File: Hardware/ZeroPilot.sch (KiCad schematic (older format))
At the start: 2 parts

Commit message: Reconfiguring pinout round 2
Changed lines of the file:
@@
-$EndSheet
-$Sheet
-S 4700 3100 1750 3100
-U 5918F046
-F0 "Sheet5918F045" 60
-F1 "STM32F7 IO.sch" 60
-F2 "PPM" I R 6450 3400 60
-F3 "OC[1..12]" O R 6450 3300 60
-F4 "TRACED" I R 6450 3700 60
-F5 "SWDIO" B R 6450 3800 60
-F6 "SWCLK" I R 6450 3900 60
-F7 "TDI" I R 6450 4000 60
-F8 "TDO" I R 6450 4100 60
-F9 "TRACECLK" I R 6450 3600 60
-F10 "NRST" I R 6450 4200 60
-F11 "I2C2_SDA" B R 6450 5350 60
-F12 "I2C2_SCL" B R 6450 5450 60
-F13 "SPI5_MISO" B L 4700 5650 60
-F14 "SPI5_MOSI" B L 4700 5750 60
-F15 "SPI5_SCK" B L 4700 5850 60
-F16 "USART2_TX" O L 4700 3400 60
-F17 "USART2_RX" I L 4700 3500 60
-F18 "SPI1_SCK" B L 4700 4800 60
-F19 "SPI1_MISO" B L 4700 4600 60
-F20 "SPI1_MOSI" B L 4700 4700 60
-F21 "I2C4_SCL" B R 6450 5750 60
-F22 "I2C4_SDA" B R 6450 5650 60
-F23 "UART7_TX" O L 4700 4350 60
-F24 "UART7_RX" I L 4700 4450 60
-F25 "SPI4_SCK" B L 4700 5500 60
-F26 "SPI4_MISO" B L 4700 5300 60
-F27 "SPI4_MOSI" B L 4700 5400 60
-F28 "USART1_RX" I L 4700 3250 60
-F29 "USART1_TX" O L 4700 3150 60
-F30 "USART3_TX" O L 4700 3750 60
-F31 "USART3_RX" I L 4700 3850 60
-F32 "USART3_CK" O L 4700 3950 60
-F33 "SPI3_SCK" B L 4700 5150 60
-F34 "SPI3_MISO" B L 4700 4950 60
-F35 "SPI3_MOSI" B L 4700 5050 60
-F36 "UART4_RX" I L 4700 4200 60
-F37 "UART4_TX" O L 4700 4100 60
-F38 "I2C1_SDA" B R 6450 5050 60
-F39 "I2C1_SCL" B R 6450 5150 60
-F40 "VDD" I R 6450 4450 60
-F41 "USART2_CK" I L 4700 3600 60
-F42 "ADC2_IN8" I R 6450 4600 60
-F43 "ADC2_IN9" I R 6450 4700 60
-F44 "ADC3_IN10" I R 6450 4800 60
-F45 "ADC3_IN11" I R 6450 4900 60
-F46 "TIM10_CH1" I R 6450 5950 60
-F47 "TIM11_CH1" I R 6450 6050 60
 $EndSheet
 $Sheet
@@
 F1 "HEADERS.sch" 60
 $EndSheet
+$Sheet
+S 4700 3100 1750 3450
+U 5918F046
+F0 "Sheet5918F045" 60
+F1 "STM32F7 IO.sch" 60
+F2 "PPM" I R 6450 3400 60
+F3 "OC[1..12]" O R 6450 3300 60
+F4 "SWDIO" B R 6450 3800 60
+F5 "SWCLK" I R 6450 3900 60
+F6 "TDI" I R 6450 4000 60
+F7 "TDO" I R 6450 4100 60
+F8 "NRST" I R 6450 4200 60
+F9 "I2C2_SDA" B R 6450 5350 60
+F10 "I2C2_SCL" B R 6450 5450 60
+F11 "I2C4_SCL" B R 6450 5750 60
+F12 "I2C4_SDA" B R 6450 5650 60
+F13 "I2C1_SDA" B R 6450 5050 60
+F14 "I2C1_SCL" B R 6450 5150 60
+F15 "VDD" I R 6450 4450 60
+F16 "ADC2_IN8" I R 6450 4600 60
+F17 "ADC2_IN9" I R 6450 4700 60
+F18 "ADC3_IN10" I R 6450 4800 60
+F19 "ADC3_IN11" I R 6450 4900 60
+F20 "TIM10_CH1" I R 6450 5950 60
+F21 "TIM11_CH1" I R 6450 6050 60
+F22 "SPI5_MISO" B L 4700 6250 60
+F23 "SPI5_MOSI" B L 4700 6350 60
+F24 "SPI5_SCK" B L 4700 6150 60
+F25 "USART2_TX" O L 4700 3150 60
+F26 "USART2_RX" I L 4700 3250 60
+F27 "SPI1_SCK" B L 4700 5150 60
+F28 "SPI1_MISO" B L 4700 5250 60
+F29 "SPI1_MOSI" B L 4700 5350 60
+F30 "UART7_TX" O L 4700 4700 60
+F31 "UART7_RX" I L 4700 4800 60
+F32 "UART1_RX" I L 4700 3900 60
+F33 "UART1_TX" O L 4700 3800 60
+F34 "USART3_TX" O L 4700 3450 60
+F35 "USART3_RX" I L 4700 3550 60
+F36 "USART3_CK" O L 4700 3650 60
+F37 "UART4_RX" I L 4700 4350 60
+F38 "UART4_TX" O L 4700 4250 60
+F39 "USART2_CK" I L 4700 3350 60
+F40 "SPI5_NSS" B L 4700 6450 60
+F41 "SPI2_MISO" B L 4700 5700 60
+F42 "SPI2_MOSI" B L 4700 5800 60
+F43 "UART4_CTS" I L 4700 4450 60
+F44 "UART7_CTS" I L 4700 4900 60
+F45 "UART7_RTS" I L 4700 5000 60
+F46 "SPI2_SCK" I L 4700 5600 60
+F47 "SPI2_NSS" I L 4700 5900 60
+F48 "UART4_RTS" I L 4700 4550 60
+F49 "UART1_CTS" I L 4700 4000 60
+F50 "UART1_RTS" I L 4700 4100 60
+F51 "SPI1_NSS" B L 4700 5450 60
+F52 "JRST" I R 6450 4300 60
+$EndSheet
 $EndSCHEMATC

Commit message: first rough draft without headers
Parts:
- added R37, R38: R, symbol R
- gave numbers to parts that had none: 2
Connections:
- net GND: now also R38.2
- net Sheet5918F045/ADC2_IN9: now also R37.2, R38.1
- new net EXT_BATT: R37.1
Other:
- note added: "TODO: Add all the headers\n(This is a lot of manual labor so \njust look at everything else first, \nthen I can connect it all to headers)\n"
- note added: "TODO: do we need these?\n"
- note added: "TODO: verify programming pinout"
- moved on the sheet: R39, R40

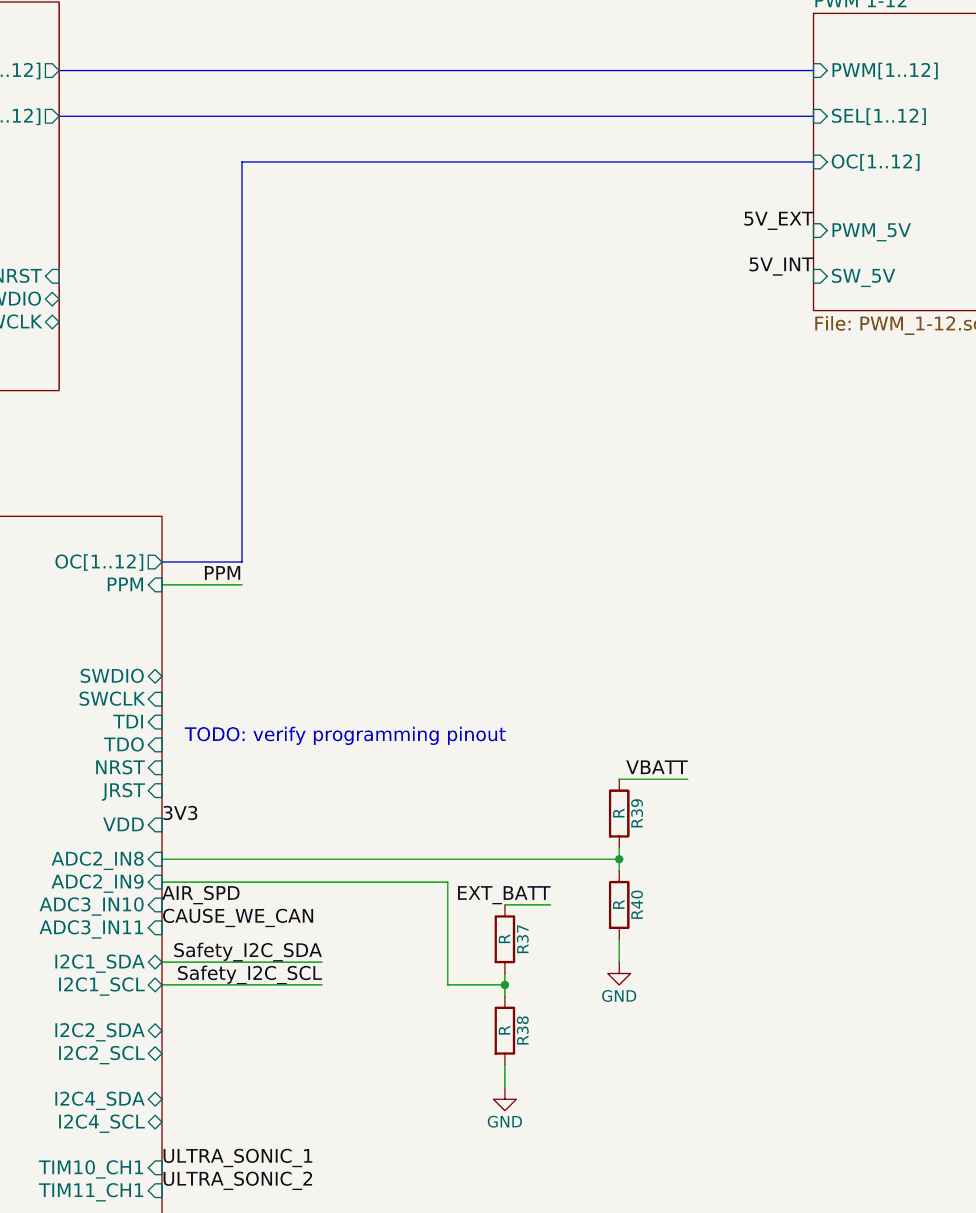
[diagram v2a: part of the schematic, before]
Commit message: branch to make PR for review
I should have made a separate branch for the development and then merged
it, but its too late now.
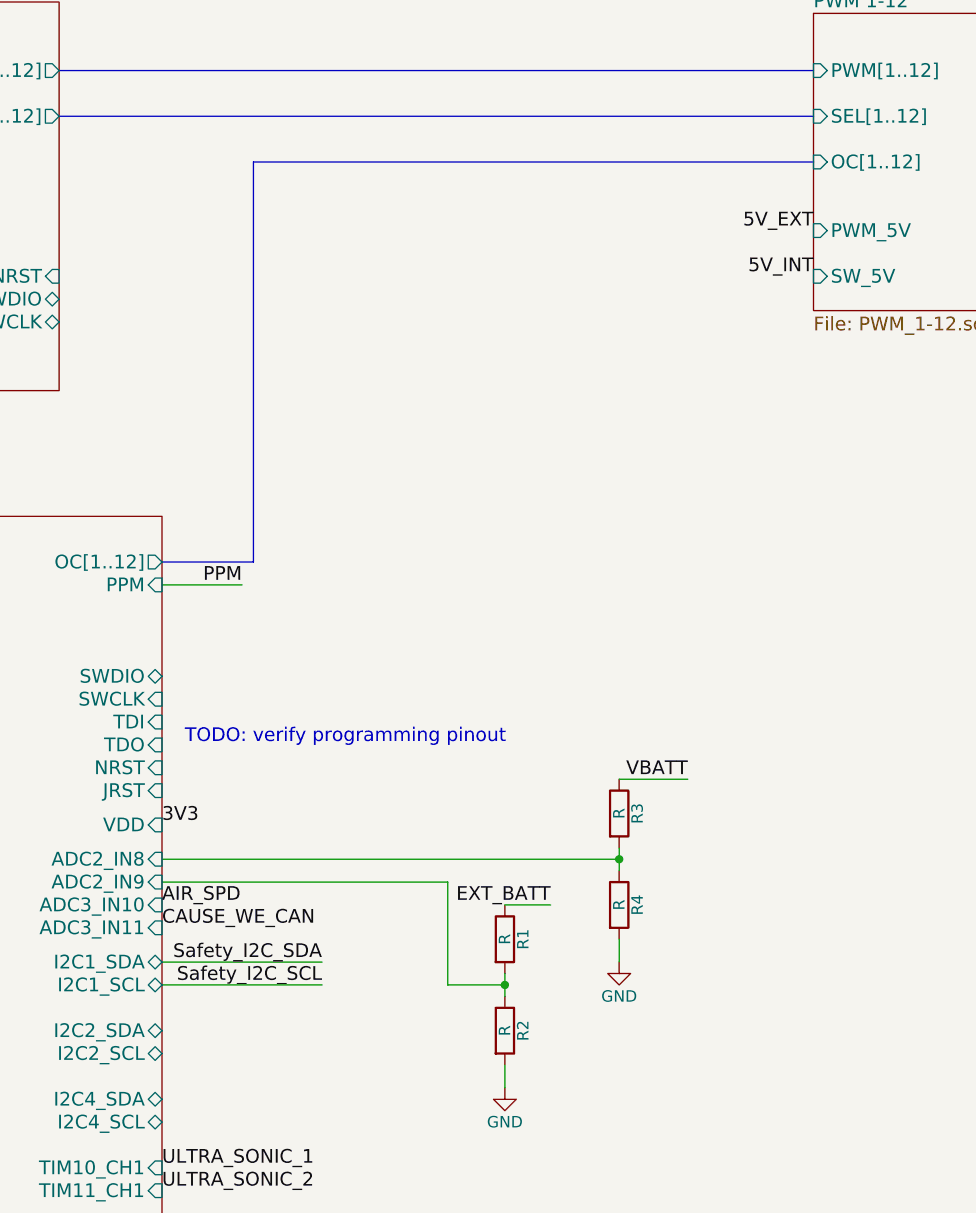
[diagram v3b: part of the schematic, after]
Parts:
- renumbered R37 to R1, R38 to R2, R39 to R3, R40 to R4
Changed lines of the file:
@@
 	6550 1150 9850 1150
 Wire Bus Line
-	7000 3100 7350 3100
+	7000 3100 7400 3100
 Wire Bus Line
-	7350 3100 7350 1350
+	7400 3100 7400 1350
 Wire Bus Line
-	7350 1350 9850 1350
+	7400 1350 9850 1350
 Wire Wire Line
 	7000 4850 7700 4850
@@
 VBATT
 $Comp
-L R R39
+L R R3
 U 1 1 5921B35E
 P 9000 4200
-F 0 "R39" V 9080 4200 50  0000 C CNN
+F 0 "R3" V 9080 4200 50  0000 C CNN
 F 1 "R" V 9000 4200 50  0000 C CNN
 F 2 "" V 8930 4200 50  0001 C CNN
@@
 $EndComp
 $Comp
-L R R40
+L R R4
 U 1 1 5921B536
 P 9000 4600
-F 0 "R40" V 9080 4600 50  0000 C CNN
+F 0 "R4" V 9080 4600 50  0000 C CNN
 F 1 "R" V 9000 4600 50  0000 C CNN
 F 2 "" V 8930 4600 50  0001 C CNN
@@
 	9300 4050 9000 4050
 $Comp
-L GND #PWR01
+L GND #PWR2
 U 1 1 5921B8F8
 P 9000 4850
-F 0 "#PWR01" H 9000 4600 50  0001 C CNN
+F 0 "#PWR2" H 9000 4600 50  0001 C CNN
 F 1 "GND" H 9000 4700 50  0000 C CNN
 F 2 "" H 9000 4850 50  0001 C CNN
@@
 	9000 4750 9000 4850
 Wire Wire Line
-	9000 4350 9000 4450
+	9000 4350 9000 4400
+Wire Wire Line
+	9000 4400 9000 4450
 Wire Wire Line
 	7000 4400 9000 4400
@@
 CAUSE_WE_CAN
 $Comp
-L R R37
+L R R1
 U 1 1 59287247
 P 8500 4750
-F 0 "R37" V 8580 4750 50  0000 C CNN
+F 0 "R1" V 8580 4750 50  0000 C CNN
 F 1 "R" V 8500 4750 50  0000 C CNN
 F 2 "" V 8430 4750 50  0001 C CNN
@@
 $EndComp
 $Comp
-L R R38
+L R R2
 U 1 1 5928724E
 P 8500 5150
-F 0 "R38" V 8580 5150 50  0000 C CNN
+F 0 "R2" V 8580 5150 50  0000 C CNN
 F 1 "R" V 8500 5150 50  0000 C CNN
 F 2 "" V 8430 5150 50  0001 C CNN
@@
 $EndComp
 $Comp
-L GND #PWR02
+L GND #PWR1
 U 1 1 59287255
 P 8500 5400
-F 0 "#PWR02" H 8500 5150 50  0001 C CNN
+F 0 "#PWR1" H 8500 5150 50  0001 C CNN
 F 1 "GND" H 8500 5250 50  0000 C CNN
 F 2 "" H 8500 5400 50  0001 C CNN
@@
 	8500 5300 8500 5400
 Wire Wire Line
-	8500 4900 8500 5000
+	8500 4900 8500 4950
+Wire Wire Line
+	8500 4950 8500 5000
 Wire Wire Line
 	8500 4950 8250 4950

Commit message: Added a lot of debug
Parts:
- added J?: CONN_01X06, symbol CONN_01X06
- added J?: CONN_01X03, symbol CONN_01X03
- added R? (x4): 0, symbol R
- added TP? (x2): TEST, symbol TEST
- 10k: renamed from R3; value R -> 10k
- R1: value R -> 100K
- R2: value R -> 22K
- R4: value R -> 3k
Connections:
- net labels added: PW_GOOD_EXT, PW_GOOD_INT
- wire segments 26 -> 38
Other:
- note removed: "TODO: do we need these?\n"
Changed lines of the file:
@@
 Text Label 2750 1100 0    60   ~ 0
 PPM
-Wire Wire Line
-	1600 2800 1850 2800
-Text Label 1850 2800 2    60   ~ 0
+Text Label 2150 2800 0    60   ~ 0
 VBATT
 Text Label 9300 4050 2    60   ~ 0
 VBATT
 $Comp
-L R R3
+L R 10k
 U 1 1 5921B35E
 P 9000 4200
-F 0 "R3" V 9080 4200 50  0000 C CNN
-F 1 "R" V 9000 4200 50  0000 C CNN
+F 0 "10k" V 9080 4200 50  0000 C CNN
+F 1 "10k" V 9000 4200 50  0000 C CNN
 F 2 "" V 8930 4200 50  0001 C CNN
 F 3 "" H 9000 4200 50  0001 C CNN
@@
 P 9000 4600
 F 0 "R4" V 9080 4600 50  0000 C CNN
-F 1 "R" V 9000 4600 50  0000 C CNN
+F 1 "3k" V 9000 4600 50  0000 C CNN
 F 2 "" V 8930 4600 50  0001 C CNN
 F 3 "" H 9000 4600 50  0001 C CNN
@@
 	9000 4750 9000 4850
 Wire Wire Line
-	9000 4350 9000 4400
-Wire Wire Line
-	9000 4400 9000 4450
+	9000 4350 9000 4450
 Wire Wire Line
 	7000 4400 9000 4400
@@
 F51 "SPI1_NSS" B L 5250 5250 60
 F52 "JRST" I R 7000 4100 60
+F53 "PG14" I R 7000 6050 60
+F54 "PG15" I R 7000 6150 60
 $EndSheet
 Text Label 4800 900  2    60   ~ 0
@@
 Text Label 7000 4250 0    60   ~ 0
 3V3
-Text Label 1600 2550 0    60   ~ 0
+Text Label 2150 2550 0    60   ~ 0
 3V3
-Text Label 1600 2150 0    60   ~ 0
+Text Label 2150 2150 0    60   ~ 0
 5V_INT
-Text Label 1600 2350 0    60   ~ 0
+Text Label 2150 2350 0    60   ~ 0
 5V_EXT
 Text Label 9850 1850 2    60   ~ 0
@@
 P 8500 4750
 F 0 "R1" V 8580 4750 50  0000 C CNN
-F 1 "R" V 8500 4750 50  0000 C CNN
+F 1 "100K" V 8500 4750 50  0000 C CNN
 F 2 "" V 8430 4750 50  0001 C CNN
 F 3 "" H 8500 4750 50  0001 C CNN
@@
 P 8500 5150
 F 0 "R2" V 8580 5150 50  0000 C CNN
-F 1 "R" V 8500 5150 50  0000 C CNN
+F 1 "22K" V 8500 5150 50  0000 C CNN
 F 2 "" V 8430 5150 50  0001 C CNN
 F 3 "" H 8500 5150 50  0001 C CNN
@@
 	8500 5300 8500 5400
 Wire Wire Line
-	8500 4900 8500 4950
-Wire Wire Line
-	8500 4950 8500 5000
+	8500 4900 8500 5000
 Wire Wire Line
 	8500 4950 8250 4950
@@
 Text Notes 1350 4900 0    60   ~ 0
 TODO: Add all the headers\n(This is a lot of manual labor so \njust look at everything else first, \nthen I can connect it all to headers)\n
-Text Notes 1600 1350 0    60   ~ 0
-TODO: do we need these?\n
+Text Label 7000 6050 0    60   ~ 0
+PW_GOOD_EXT
+Text Label 7000 6150 0    60   ~ 0
+PW_GOOD_INT
+Text Label 1600 1500 0    60   ~ 0
+PW_GOOD_INT
+Text Label 1600 1300 0    60   ~ 0
+PW_GOOD_EXT
+$Comp
+L CONN_01X06 J?
+U 1 1 592CD4C4
+P 3150 2350
+F 0 "J?" H 3150 2700 50  0000 C CNN
+F 1 "CONN_01X06" V 3250 2350 50  0000 C CNN
+F 2 "" H 3150 2350 50  0001 C CNN
+F 3 "" H 3150 2350 50  0001 C CNN
+	1    3150 2350
+	1    0    0    -1
+$EndComp
+Text Label 2950 2100 2    60   ~ 0
+5V_INT
+Text Label 2950 2200 2    60   ~ 0
+5V_EXT
+Text Label 2950 2300 2    60   ~ 0
+3V3
+Text Label 2950 2400 2    60   ~ 0
+VBATT
+$Comp
+L GND #PWR?
+U 1 1 592CE3A7
+P 2850 2800
+F 0 "#PWR?" H 2850 2550 50  0001 C CNN
+F 1 "GND" H 2850 2650 50  0000 C CNN
+F 2 "" H 2850 2800 50  0001 C CNN
+F 3 "" H 2850 2800 50  0001 C CNN
+	1    2850 2800
+	1    0    0    -1
+$EndComp
+Wire Wire Line
+	2950 2500 2850 2500
+Wire Wire Line
+	2850 2500 2850 2800
+Wire Wire Line
+	2950 2600 2850 2600
+Connection ~ 2850 2600
+$Comp
+L R R?
+U 1 1 592CFA5D
+P 1850 2800
+F 0 "R?" V 1930 2800 50  0000 C CNN
+F 1 "0" V 1850 2800 50  0000 C CNN
+F 2 "" V 1780 2800 50  0001 C CNN
+F 3 "" H 1850 2800 50  0001 C CNN
+	1    1850 2800
+	0    1    1    0
+$EndComp
+$Comp
+L R R?
+U 1 1 592CFDC0
+P 1850 2550
+F 0 "R?" V 1930 2550 50  0000 C CNN
+F 1 "0" V 1850 2550 50  0000 C CNN
+F 2 "" V 1780 2550 50  0001 C CNN
+F 3 "" H 1850 2550 50  0001 C CNN
+	1    1850 2550
+	0    1    1    0
+$EndComp
+$Comp
+L R R?
+U 1 1 592CFFFF
+P 1850 2350
+F 0 "R?" V 1930 2350 50  0000 C CNN
+F 1 "0" V 1850 2350 50  0000 C CNN
+F 2 "" V 1780 2350 50  0001 C CNN
+F 3 "" H 1850 2350 50  0001 C CNN
+	1    1850 2350
+	0    1    1    0
+$EndComp
+$Comp
+L R R?
+U 1 1 592D023F
+P 1850 2150
+F 0 "R?" V 1930 2150 50  0000 C CNN
+F 1 "0" V 1850 2150 50  0000 C CNN
+F 2 "" V 1780 2150 50  0001 C CNN
+F 3 "" H 1850 2150 50  0001 C CNN
+	1    1850 2150
+	0    1    1    0
+$EndComp
+Wire Wire Line
+	1700 2150 1600 2150
+Wire Wire Line
+	1700 2350 1600 2350
+Wire Wire Line
+	1600 2550 1700 2550
+Wire Wire Line
+	1700 2800 1600 2800
+Wire Wire Line
+	2000 2800 2150 2800
+Wire Wire Line
+	2150 2550 2000 2550
+Wire Wire Line
+	2000 2350 2150 2350
+Wire Wire Line
+	2150 2150 2000 2150
+Wire Wire Line
+	1600 1300 2300 1300
+Wire Wire Line
+	1600 1500 2450 1500
+$Comp
+L TEST TP?
+U 1 1 592D52D6
+P 2300 1300
+F 0 "TP?" H 2300 1600 50  0000 C BNN
+F 1 "TEST" H 2300 1550 50  0000 C CNN
+F 2 "" H 2300 1300 50  0001 C CNN
+F 3 "" H 2300 1300 50  0001 C CNN
+	1    2300 1300
+	1    0    0    -1
+$EndComp
+$Comp
+L TEST TP?
+U 1 1 592D5525
+P 2450 1500
+F 0 "TP?" H 2450 1800 50  0000 C BNN
+F 1 "TEST" H 2450 1750 50  0000 C CNN
+F 2 "" H 2450 1500 50  0001 C CNN
+F 3 "" H 2450 1500 50  0001 C CNN
+	1    2450 1500
+	1    0    0    -1
+$EndComp
+$Comp
+L CONN_01X03 J?
+U 1 1 592DED76
+P 3800 2100
+F 0 "J?" H 3800 2300 50  0000 C CNN
+F 1 "CONN_01X03" V 3900 2100 50  0000 C CNN
+F 2 "" H 3800 2100 50  0001 C CNN
+F 3 "" H 3800 2100 50  0001 C CNN
+	1    3800 2100
+	-1   0    0    1
+$EndComp
+Wire Wire Line
+	4000 2200 4100 2200
+Wire Wire Line
+	4100 2200 4100 2300
+$Comp
+L GND #PWR?
+U 1 1 592DF11B
+P 4100 2300
+F 0 "#PWR?" H 4100 2050 50  0001 C CNN
+F 1 "GND" H 4100 2150 50  0000 C CNN
+F 2 "" H 4100 2300 50  0001 C CNN
+F 3 "" H 4100 2300 50  0001 C CNN
+	1    4100 2300
+	1    0    0    -1
+$EndComp
 $EndSCHEMATC

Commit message: Fixed some BOM stuff
fixed BOM for non RLC components
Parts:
- removed J?: CONN_01X06, symbol CONN_01X06
- removed R? (x4): 0, symbol R
- added D1, D2: D, symbol D
- added J2: CONN_01X04, symbol CONN_01X04
- added R1, R2: 0, symbol R
- J1: renamed from J?; part_num (none) -> CONN-007
- gave numbers to parts that had none: 2
- renumbered R1 to R3, R2 to R4, 10k to R5, R4 to R6
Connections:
- net labels added: CTS1, CTS2, CTS4, CTS7, I2C, MEM_WC, MISO1, MISO2, MISO4, MISO5, MOSI1, MOSI2, MOSI4, MOSI5, NRST_PILOT, NRST_SAFETY, NSS1, NSS2, NSS4, NSS5, PPM_BUFF, REC_RX, RTS1, RTS2, RTS4, RTS7, RX1, RX2, RX3, RX4, RX7, SAFETY_DBG_RX, SAFETY_DBG_TX, SCK1, SCK2, SCK4, SCK5, SCL1, SCL2, SCL4, SCLK_PILOT, SCLK_SAFETY, SDA1, SDA2, SDA4, SPI, SWIO_PILOT, SWIO_SAFETY, TX1, TX2, TX3, TX4, TX7, UART, UCK2, UCK3
- net labels removed: CAUSE_WE_CAN, Safety_I2C_SCL, Safety_I2C_SDA
- wire segments 38 -> 139
- no-connect marks 0 -> 2
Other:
- note added: "Reserved lines:\nI2C1: flash memory and safety controller\nSPI5: SD card\nUART3: debug\nUART7: Reciever uart"
- note removed: "TODO: Add all the headers\n(This is a lot of manual labor so \njust look at everything else first, \nthen I can connect it all to headers)\n"
- note removed: "TODO: verify programming pinout"
- moved on the sheet: J1, R3, R4, R5, R6

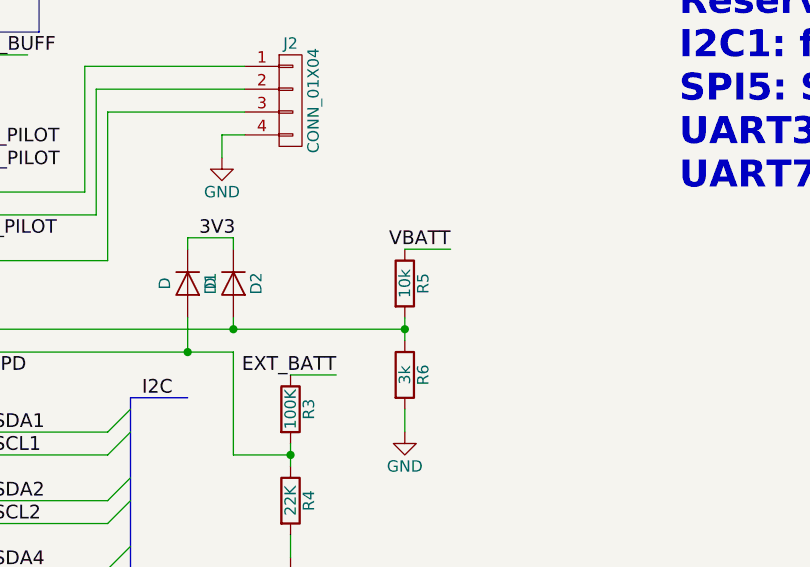
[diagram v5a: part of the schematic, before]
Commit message: Finished RLC bom stuff
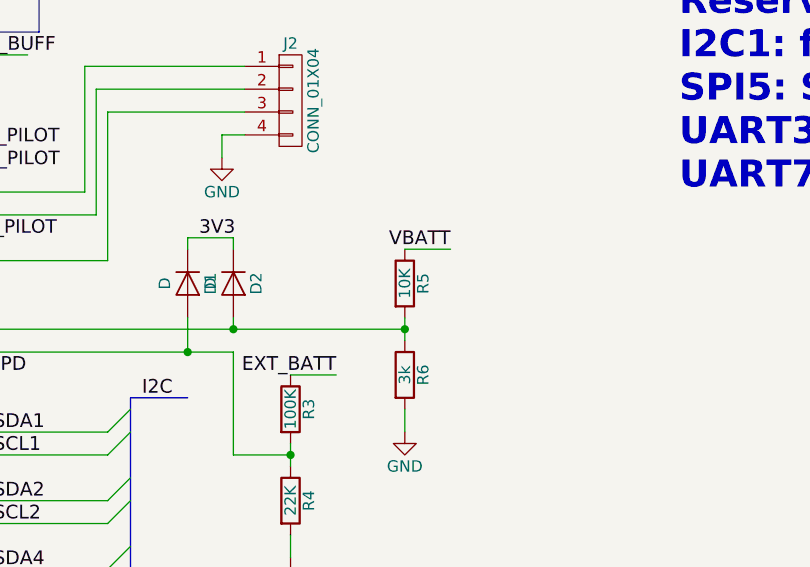
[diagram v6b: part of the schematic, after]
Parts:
- D1, D2: part_num (none) -> DIOD-004
- R1, R2: part_num (none) -> RESS-001
- R3: part_num (none) -> RESS-003
- R4: part_num (none) -> RESS-002
- R5: value 10k -> 10K; part_num (none) -> RESS-005
- R6: part_num (none) -> RESS-004
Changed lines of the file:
@@
 P 10950 3550
 F 0 "R5" V 11030 3550 50  0000 C CNN
-F 1 "10k" V 10950 3550 50  0000 C CNN
+F 1 "10K" V 10950 3550 50  0000 C CNN
 F 2 "" V 10880 3550 50  0001 C CNN
 F 3 "" H 10950 3550 50  0001 C CNN
+F 4 "RESS-005" V 10950 3550 60  0001 C CNN "part_num"
 	1    10950 3550
 	1    0    0    -1
@@
 F 2 "" V 10880 3950 50  0001 C CNN
 F 3 "" H 10950 3950 50  0001 C CNN
+F 4 "RESS-004" V 10950 3950 60  0001 C CNN "part_num"
 	1    10950 3950
 	1    0    0    -1
@@
 F 2 "" V 10380 4100 50  0001 C CNN
 F 3 "" H 10450 4100 50  0001 C CNN
+F 4 "RESS-003" V 10450 4100 60  0001 C CNN "part_num"
 	1    10450 4100
 	1    0    0    -1
@@
 F 2 "" V 10380 4500 50  0001 C CNN
 F 3 "" H 10450 4500 50  0001 C CNN
+F 4 "RESS-002" V 10450 4500 60  0001 C CNN "part_num"
 	1    10450 4500
 	1    0    0    -1
@@
 F 2 "" V 3980 2000 50  0001 C CNN
 F 3 "" H 4050 2000 50  0001 C CNN
+F 4 "RESS-001" V 4050 2000 60  0001 C CNN "part_num"
 	1    4050 2000
 	0    1    1    0
@@
 F 2 "" V 3980 2100 50  0001 C CNN
 F 3 "" H 4050 2100 50  0001 C CNN
+F 4 "RESS-001" V 4050 2100 60  0001 C CNN "part_num"
 	1    4050 2100
 	0    1    1    0
@@
 F 2 "" H 10000 3550 50  0001 C CNN
 F 3 "" H 10000 3550 50  0001 C CNN
+F 4 "DIOD-004" H 10000 3550 60  0001 C CNN "part_num"
 	1    10000 3550
 	0    1    1    0
@@
 F 2 "" H 10200 3550 50  0001 C CNN
 F 3 "" H 10200 3550 50  0001 C CNN
+F 4 "DIOD-004" H 10200 3550 60  0001 C CNN "part_num"
 	1    10200 3550
 	0    1    1    0
